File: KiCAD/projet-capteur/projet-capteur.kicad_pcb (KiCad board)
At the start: 2 copper layers, 68.6 x 53.3 mm, 25 parts, among them J1 Power, J2 Analog, J3 Digital/PWM, J4 Digital/PWM, U2 LTC1050

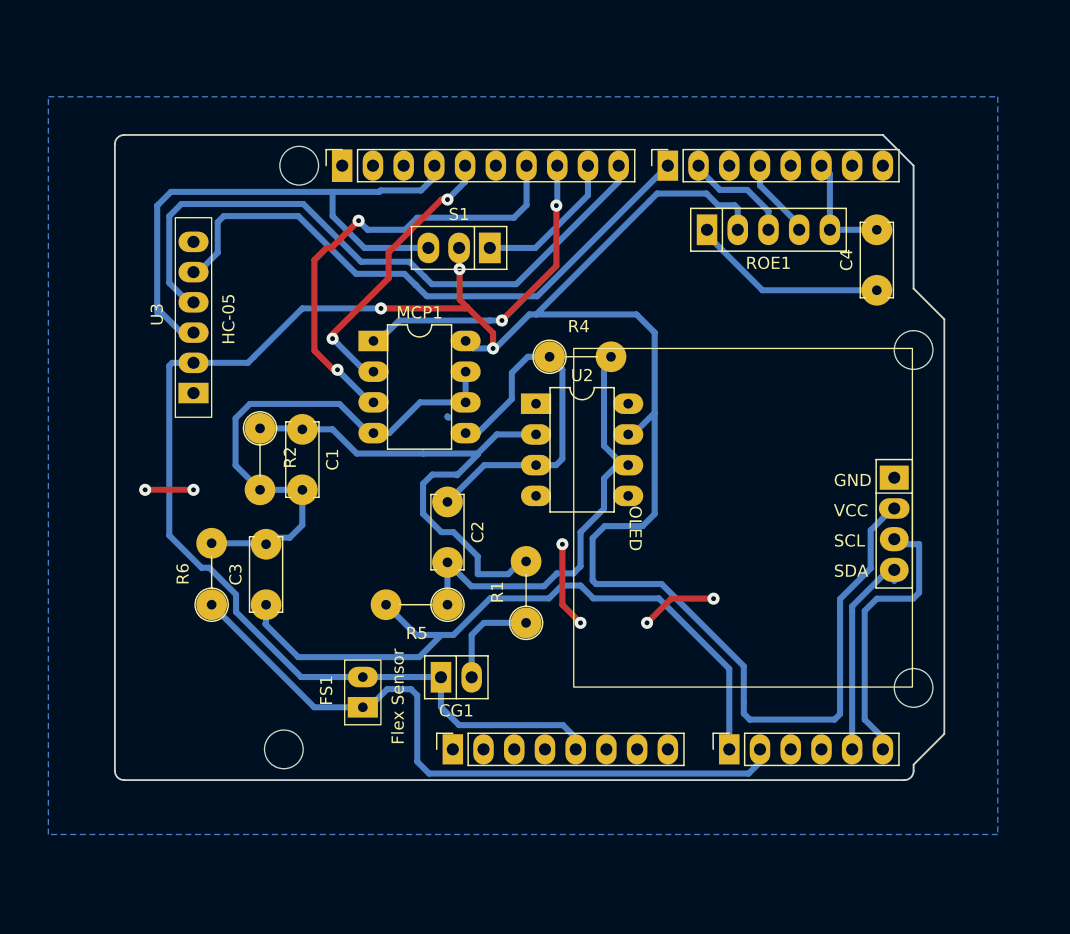
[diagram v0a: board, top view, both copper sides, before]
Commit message: Changement des positions du encodeur
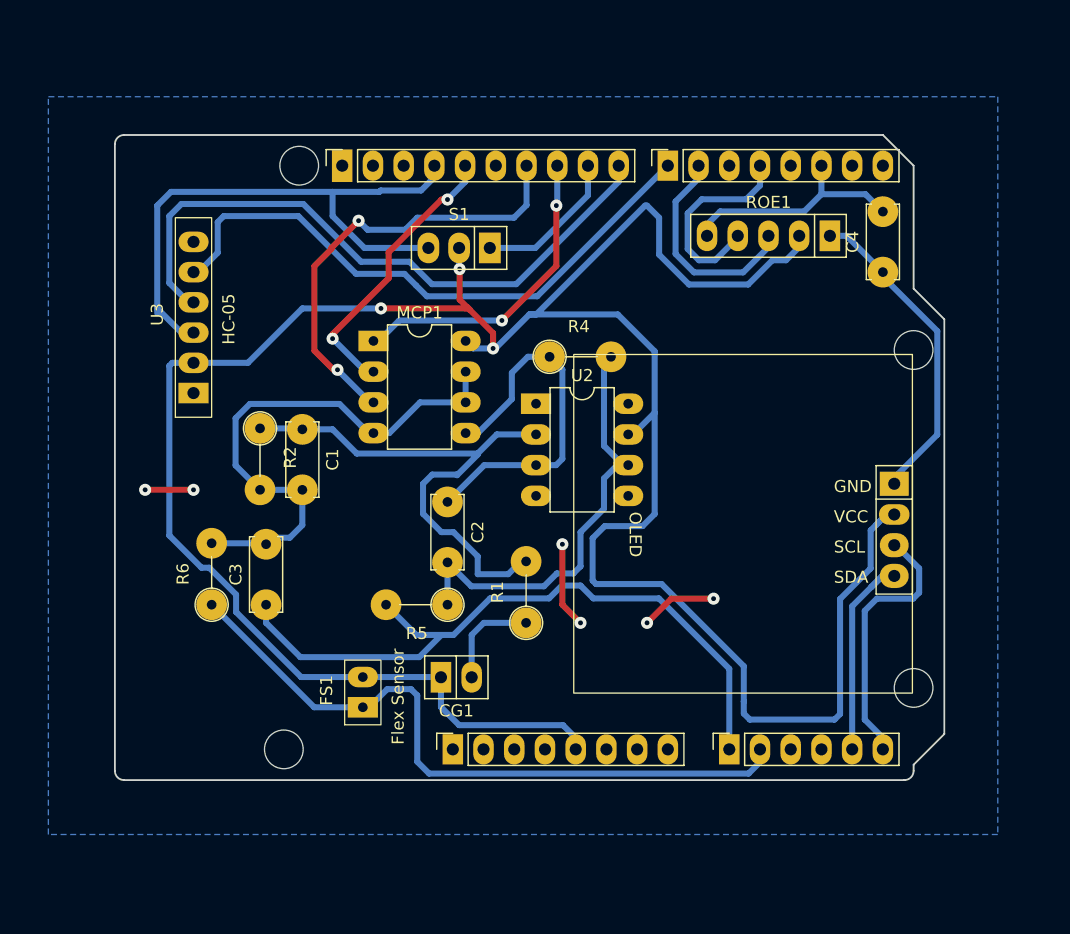
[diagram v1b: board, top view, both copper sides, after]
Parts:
- moved C4 1.58 mm to (163.5, 58.0)
- moved ROE1 0.50 mm to (154.0, 55.0), turned to 180 degrees
- moved U1 0.50 mm to (164.4, 79.3)
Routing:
- net 5V: track 208.7 -> 221.5 mm
- net ROE 4: track 6.64 -> 17.0 mm
- net GND: track 128.1 -> 138.0 mm
- net ROE 5: track 10.4 -> 19.9 mm
- net ROE 3: track 9.02 -> 18.2 mm
- net SCL: track 23.4 -> 22.1 mm
- net ADC: track 59.5 -> 58.6 mm
- net SDA: track 18.2 -> 18.8 mm

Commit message: Seance Realisation du shield 13.03
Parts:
- moved C3 37.5 mm to (150.0, 84.0), turned to -90 degrees
- moved C2 30.9 mm to (155.0, 63.0), turned to 180 degrees
- moved R5 28.0 mm to (155.0, 80.0)
- moved R4 19.2 mm to (155.0, 67.5), turned to -90 degrees
- moved U2 2.37 mm to (137.2, 68.9)
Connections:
- C1 pad 1: Net-(U2--) -> Net-(U2-+)
- R1 pad 2: Net-(U2--) -> Net-(U2-+)
- R2 pad 1: Net-(U2--) -> Net-(U2-+)
- U2 pad 1: (no net) -> unconnected-(U2-NC-Pad1)
- U2 pad 2: Net-(U2--) -> R3
- U2 pad 3: R3 -> Net-(U2-+)
- U2 pad 5: (no net) -> unconnected-(U2-EXT_CLK-Pad5)
- U2 pad 8: (no net) -> unconnected-(U2-NC-Pad8)
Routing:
- net Net-(U2--): track 44.4 -> 0.00 mm
- net ADC: track 58.6 -> 18.8 mm
- net Net-(U2-+): track 0.00 -> 34.7 mm
- net 5V: track 221.5 -> 189.8 mm, vias 3 -> 4
- net R3: track 30.7 -> 44.0 mm
- net GND: track 138.0 -> 128.1 mm, vias 6 -> 0
- net SDA: track 18.8 -> 16.4 mm
- net Net-(C2-Pad2): track 36.8 -> 38.3 mm
- net /*11: track 37.2 -> 36.4 mm

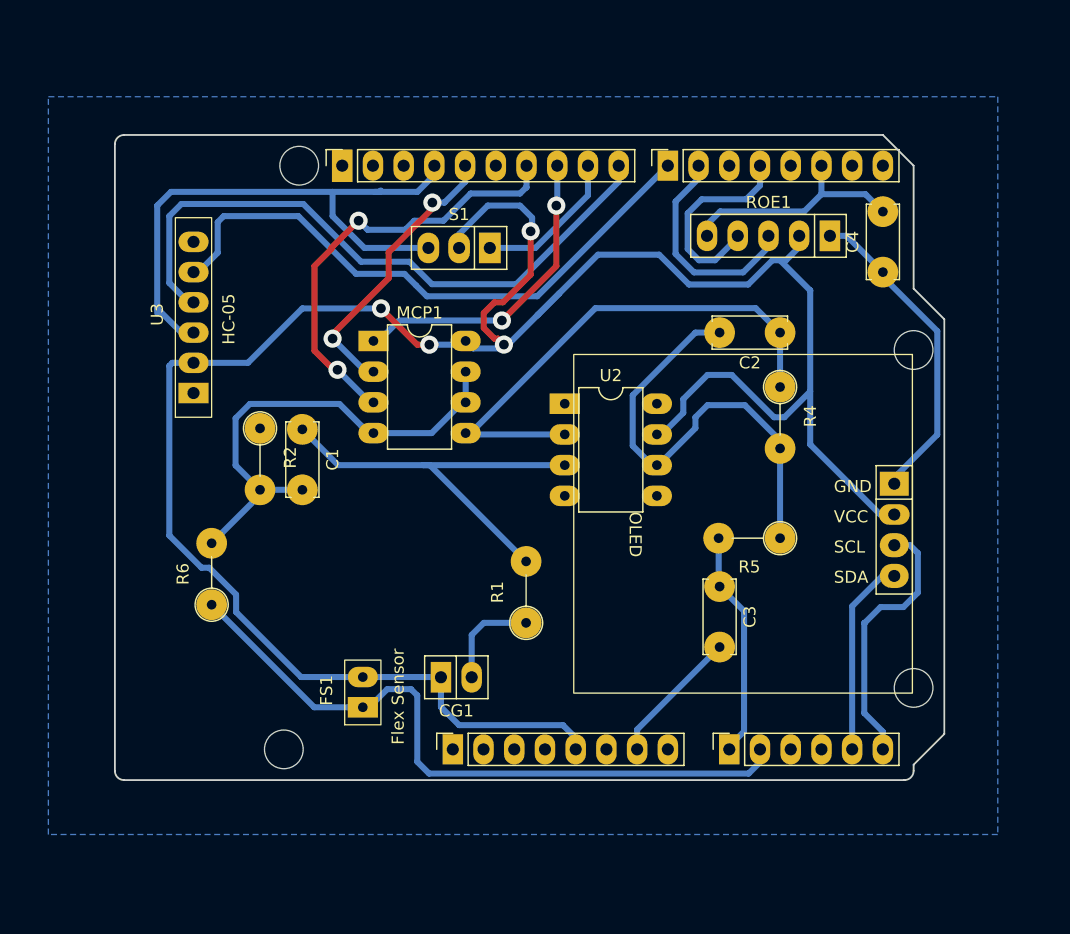
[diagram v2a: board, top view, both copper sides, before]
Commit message: Modif des tracks + pins
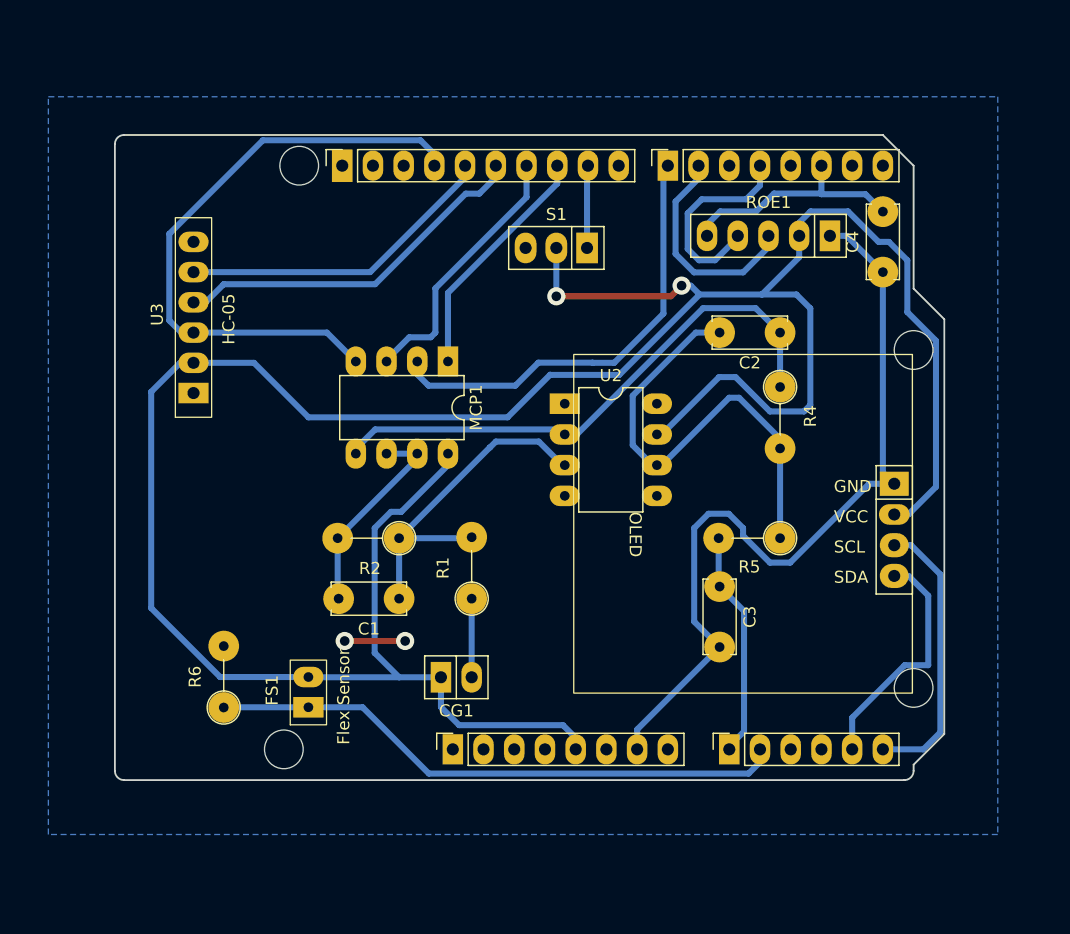
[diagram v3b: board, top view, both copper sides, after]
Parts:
- moved C1 16.1 mm to (123.5, 85.0), turned to 180 degrees
- moved R2 14.7 mm to (123.5, 80.0), turned to 180 degrees
- moved R6 8.56 mm to (109.0, 94.0)
- moved S1 8.04 mm to (136.5, 56.0)
- moved MCP1 6.39 mm to (127.5, 65.4), turned to -90 degrees
- moved R1 4.92 mm to (129.5, 85.0)
- moved FS1 4.50 mm to (116.0, 92.6)
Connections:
- J3 pad 10: TX -> /8
- J3 pad 5: /13 -> RX
- J3 pad 6: /12 -> TX
- J4 pad 1: RX -> /7
- MCP1 pad 2: /13 -> /7
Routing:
- net 5V: track 189.8 -> 228.5 mm, vias 4 -> 2
- net /7: track 0.00 -> 36.7 mm
- net /13: track 23.9 -> 0.00 mm, vias 2 -> 0
- net RX: track 49.8 -> 26.7 mm
- net TX: track 53.4 -> 30.2 mm
- net /*11: track 36.4 -> 22.0 mm, vias 2 -> 0
- net GND: track 128.1 -> 142.4 mm, vias 0 -> 2
- net Sortie Flex: track 57.0 -> 48.1 mm
- net /*10: track 25.9 -> 19.9 mm, vias 2 -> 0
- net Net-(U2-+): track 34.7 -> 28.8 mm
- net /*9: track 12.4 -> 6.83 mm
- net SDA: track 16.4 -> 19.9 mm
- net R3: track 44.0 -> 46.0 mm
- net Sortie Capteur: track 8.41 -> 6.50 mm
- net SCL: track 22.1 -> 23.2 mm

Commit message: Reparation des pins du potentiometre
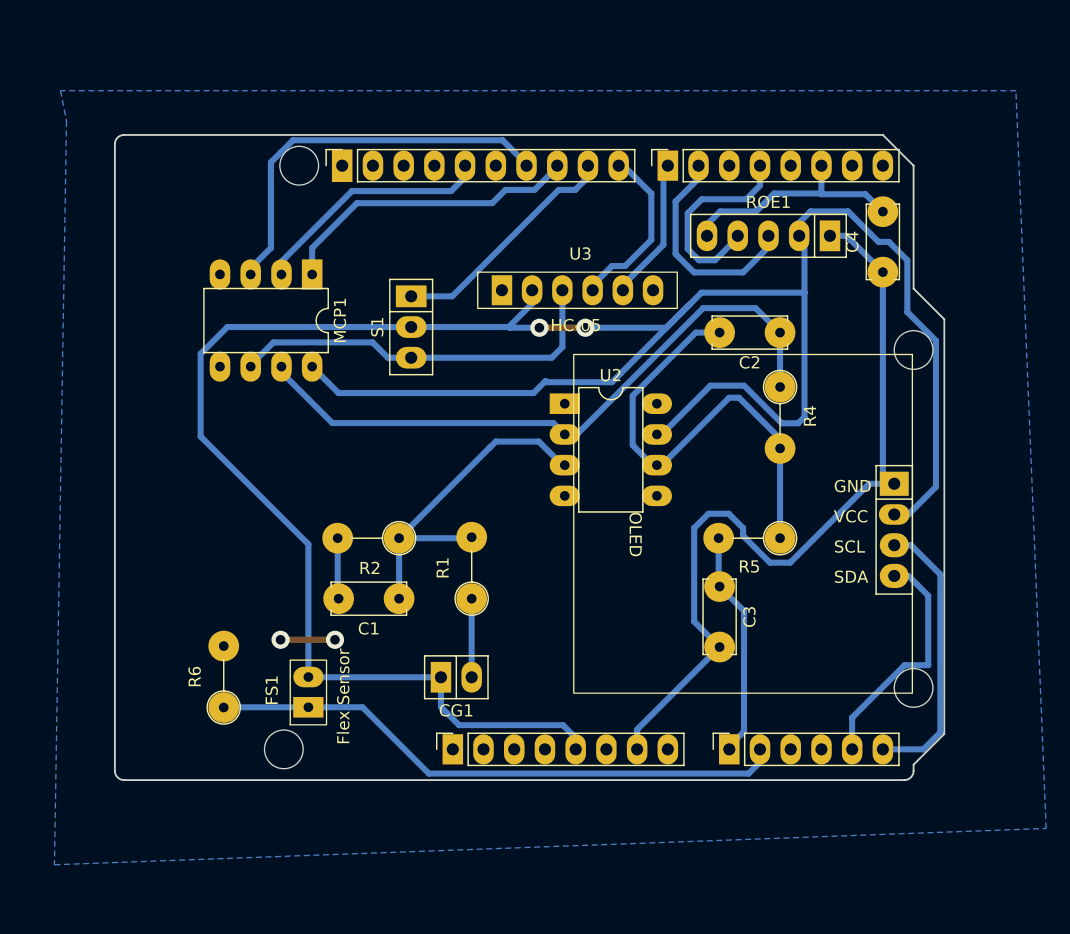
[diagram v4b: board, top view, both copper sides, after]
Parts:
- moved U3 32.1 mm to (138.5, 59.5), turned to 0 degrees
- moved S1 13.7 mm to (124.5, 62.5), turned to -90 degrees
- moved MCP1 13.3 mm to (116.3, 58.2)
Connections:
- J3 pad 10: /8 -> TX
- J3 pad 5: RX -> /13
- J3 pad 6: TX -> /12
- J4 pad 1: /7 -> RX
- MCP1 pad 2: /7 -> /13
- MCP1 pad 5: R3 -> GND
- MCP1 pad 7: GND -> R3
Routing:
- net /7: track 36.7 -> 0.00 mm
- net GND: track 142.4 -> 110.3 mm
- net /13: track 0.00 -> 20.1 mm
- net TX: track 30.2 -> 14.3 mm
- net RX: track 26.7 -> 11.8 mm
- net /*9: track 6.83 -> 19.6 mm
- net 5V: track 228.5 -> 216.3 mm
- net /*11: track 22.0 -> 32.8 mm
- net R3: track 46.0 -> 53.5 mm
- net /*10: track 19.9 -> 25.3 mm

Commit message: Correction du Bluetooth
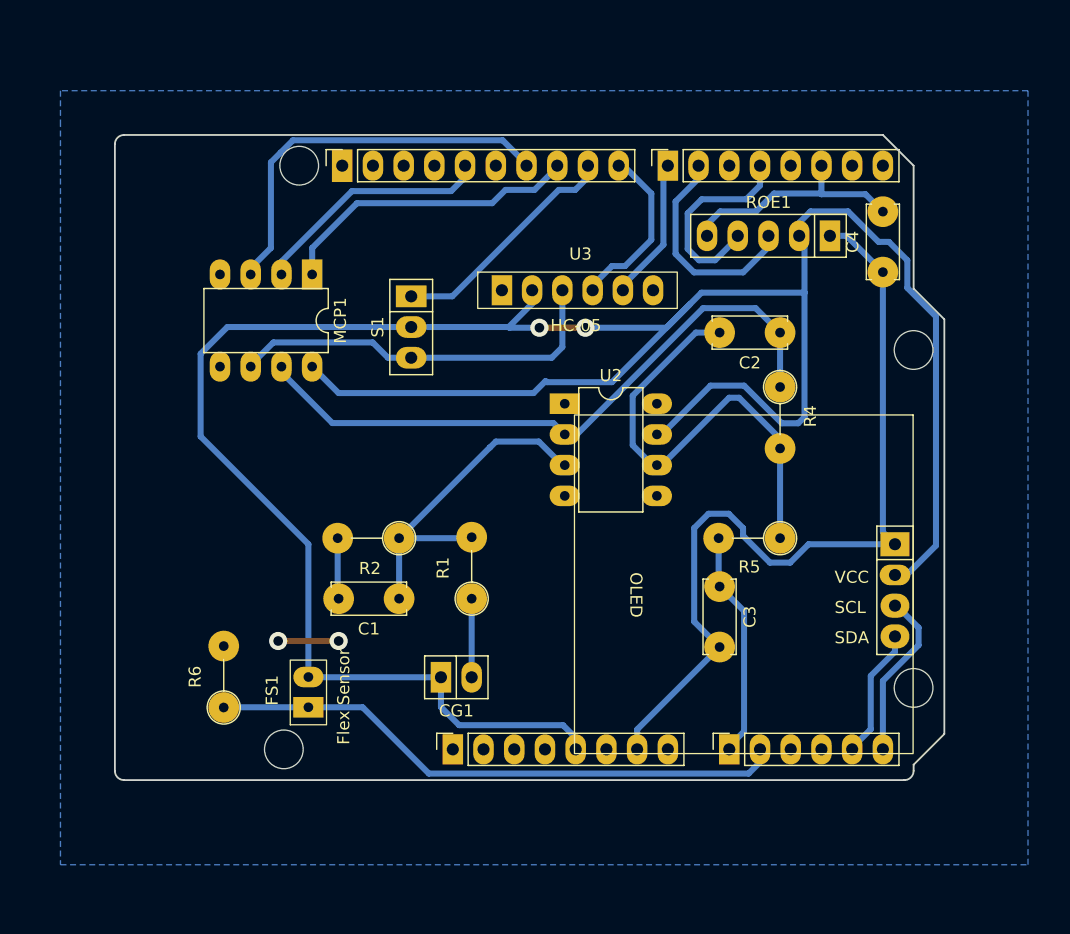
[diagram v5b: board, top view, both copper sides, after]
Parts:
- moved U1 5.00 mm to (164.5, 84.3)
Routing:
- net SCL: track 23.2 -> 14.0 mm
- net SDA: track 19.9 -> 10.8 mm
- net 5V: track 216.3 -> 221.1 mm
- net GND: track 110.3 -> 112.6 mm

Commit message: Seance Realisation banc de test 17.03
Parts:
- C4: value C -> 100n
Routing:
- net 5V: track 221.1 -> 217.1 mm
- net Net-(C2-Pad2): track 38.2 -> 36.7 mm
- net R3: track 53.5 -> 52.0 mm
- net ROE 5: track 19.9 -> 18.6 mm
- net /13: track 20.1 -> 19.1 mm
- net /*9: track 19.6 -> 18.7 mm
- net ROE 3: track 18.2 -> 17.3 mm
- net RX: track 11.8 -> 10.9 mm
- net TX: track 14.3 -> 13.5 mm
- net /*11: track 32.8 -> 32.1 mm

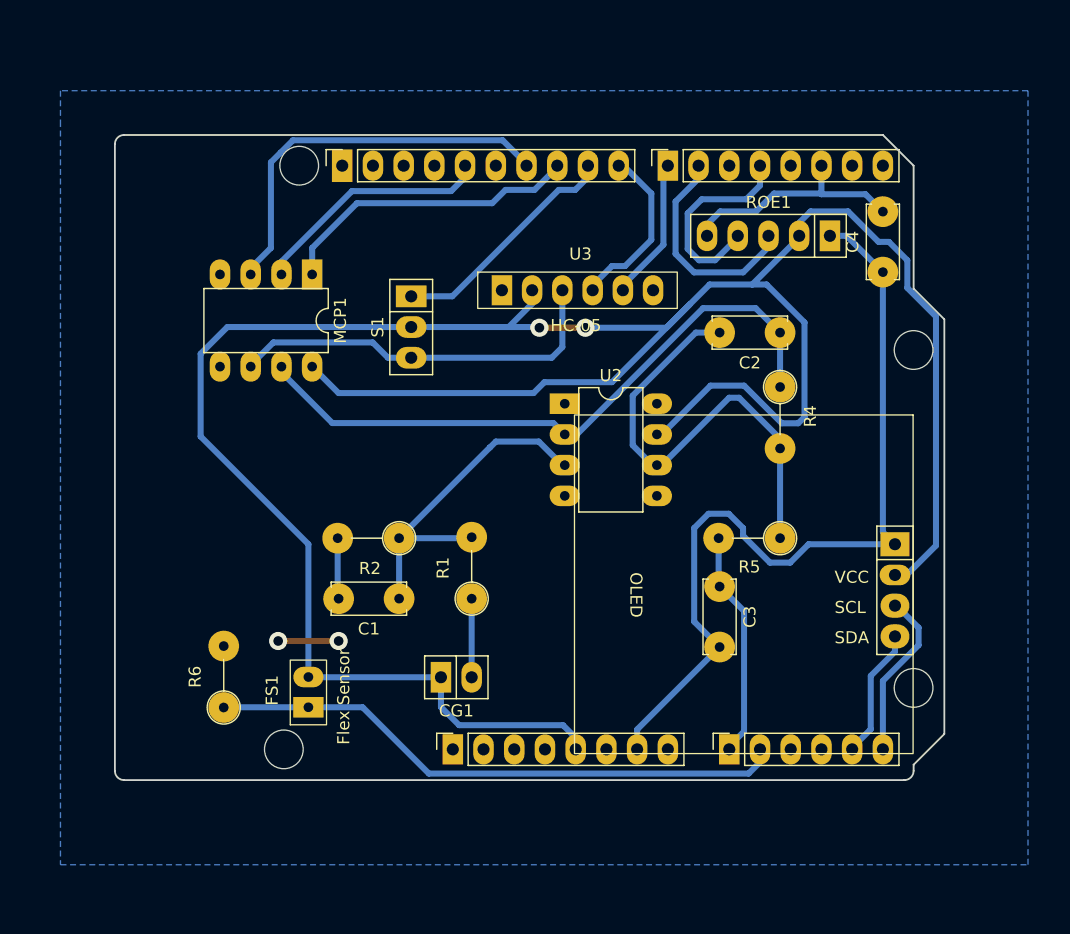
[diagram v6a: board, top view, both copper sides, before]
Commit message: Grandissement du shield
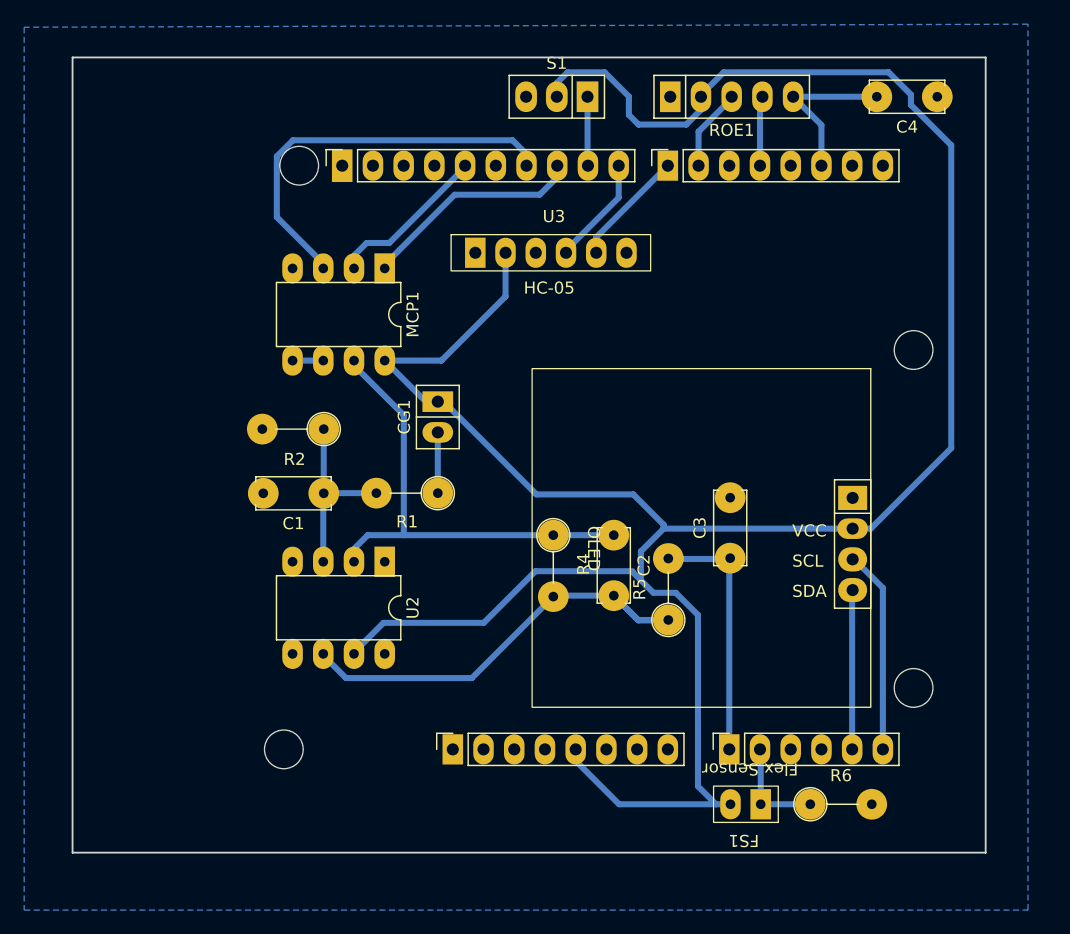
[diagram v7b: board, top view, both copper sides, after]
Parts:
- moved R6 49.2 mm to (157.5, 102.0), turned to 0 degrees
- moved FS1 37.2 mm to (152.0, 102.0), turned to 180 degrees
- moved S1 22.5 mm to (136.5, 43.5), turned to 180 degrees
- moved R4 22.4 mm to (136.2, 79.8)
- moved C2 21.7 mm to (141.2, 79.8), turned to -90 degrees
- moved CG1 21.6 mm to (126.7, 70.0), turned to -90 degrees
- moved U2 19.8 mm to (122.3, 81.9), turned to -90 degrees
- moved C4 15.2 mm to (168.0, 43.5), turned to 180 degrees
- moved ROE1 11.9 mm to (151.0, 43.5), turned to 0 degrees
- moved R5 11.4 mm to (145.8, 86.8), turned to 90 degrees
- moved R2 11.0 mm to (117.3, 71.0)
- moved C1 10.7 mm to (117.3, 76.3)
- moved R1 9.16 mm to (126.7, 76.3), turned to 180 degrees
- moved MCP1 6.02 mm to (122.3, 57.7)
- moved U1 5.19 mm to (161.0, 80.5)
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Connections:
- net Net-(C2-Pad2) renamed /AO Out
- net Net-(U2-+) renamed /AO+
- net Sortie Capteur renamed Out Sensor
- net Sortie Flex renamed Out Flex
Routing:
- net GND: track 112.4 -> 2.54 mm, vias 2 -> 0
- net Out Flex: track 48.0 -> 8.58 mm
- net /AO+: track 28.5 -> 15.3 mm
- net R3: track 52.0 -> 38.8 mm
- net /*9: track 18.7 -> 5.66 mm
- net 5V: track 217.1 -> 205.4 mm, vias 2 -> 0
- net ROE 4: track 16.8 -> 5.50 mm
- net ROE 3: track 17.3 -> 6.69 mm
- net /*10: track 25.2 -> 17.3 mm
- net /13: track 19.1 -> 13.3 mm
- net ROE 5: track 18.6 -> 13.6 mm
- net TX: track 13.5 -> 8.81 mm
- net SCL: track 13.9 -> 16.7 mm
- net SDA: track 10.7 -> 13.1 mm
- net /AO Out: track 36.7 -> 39.1 mm
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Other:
- board size 68.6 x 53.3 mm -> 75.5 x 65.8 mm
